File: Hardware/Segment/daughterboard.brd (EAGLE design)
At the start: 210.8 x 51.8 mm, 162 parts, among them IC1 PBQ79656PAPTQ1, IC2 PBQ79656PAPTQ1, T1 PBHV8115X, 115, T2 PBHV8115X, 115

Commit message: teensy.lbr
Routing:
- net CB5: track 53.4 -> 56.8 mm
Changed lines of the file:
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@@
 <attribute name="POPULARITY" value="73" x="174.117" y="67.31" size="1.778" layer="27" rot="R90" display="off"/>
 <attribute name="SPICEPREFIX" value="C" x="174.117" y="67.31" size="1.778" layer="27" rot="R90" display="off"/>
-<attribute name="VALUE" x="165.862" y="283.845" size="1.27" layer="27" rot="R90"/>
+<attribute name="VALUE" x="83.312" y="14.605" size="1.27" layer="27" rot="R90"/>
 </element>
 <element name="CAVDD" library="rcl" library_urn="urn:adsk.eagle:library:334" package="C0603" package3d_urn="urn:adsk.eagle:package:23616/2" value="1uf" x="85.725" y="18.415" smashed="yes" rot="R90">
@@
 <attribute name="POPULARITY" value="73" x="76.2" y="120.65" size="1.778" layer="27" rot="R180" display="off"/>
 <attribute name="SPICEPREFIX" value="C" x="76.2" y="120.65" size="1.778" layer="27" rot="R180" display="off"/>
-<attribute name="VALUE" x="-140.335" y="112.395" size="1.27" layer="27" rot="R180"/>
+<attribute name="VALUE" x="123.825" y="32.385" size="1.27" layer="27" rot="R180"/>
 </element>
 <element name="CAVDD-1" library="rcl" library_urn="urn:adsk.eagle:library:334" package="C0603" package3d_urn="urn:adsk.eagle:package:23616/2" value="1uf" x="125.095" y="33.655" smashed="yes">
@@
 <wire x1="68.453" y1="13.843" x2="67.6186" y2="14.9314" width="0.1524" layer="1"/>
 <wire x1="67.6186" y1="14.9314" x2="67.6186" y2="14.9946875" width="0.1524" layer="1"/>
-<wire x1="67.6186" y1="14.9946875" x2="66.04" y2="16.5732875" width="0.1524" layer="1"/>
-<wire x1="66.04" y1="24.55" x2="66.89" y2="25.4" width="0.1524" layer="1"/>
-<wire x1="66.04" y1="16.5732875" x2="66.04" y2="24.55" width="0.1524" layer="1"/>
+<wire x1="67.6186" y1="14.9946875" x2="62.05164375" y2="20.56164375" width="0.1524" layer="1"/>
+<wire x1="62.05164375" y1="20.56164375" x2="66.89" y2="25.4" width="0.1524" layer="1"/>
 </signal>
 <signal name="VC6">

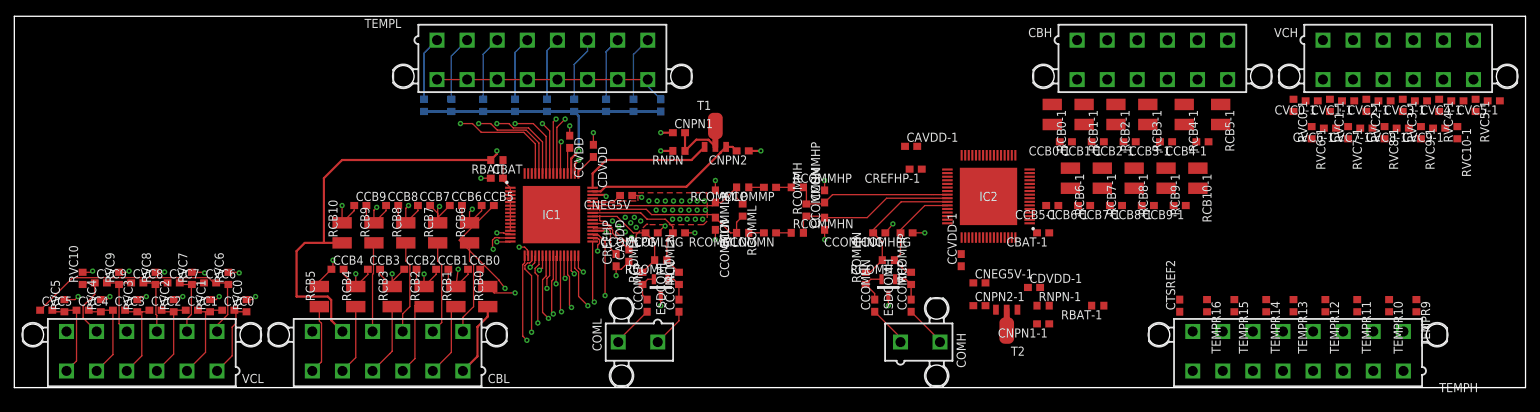
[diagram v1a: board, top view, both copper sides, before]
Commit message: Ground planes on segment
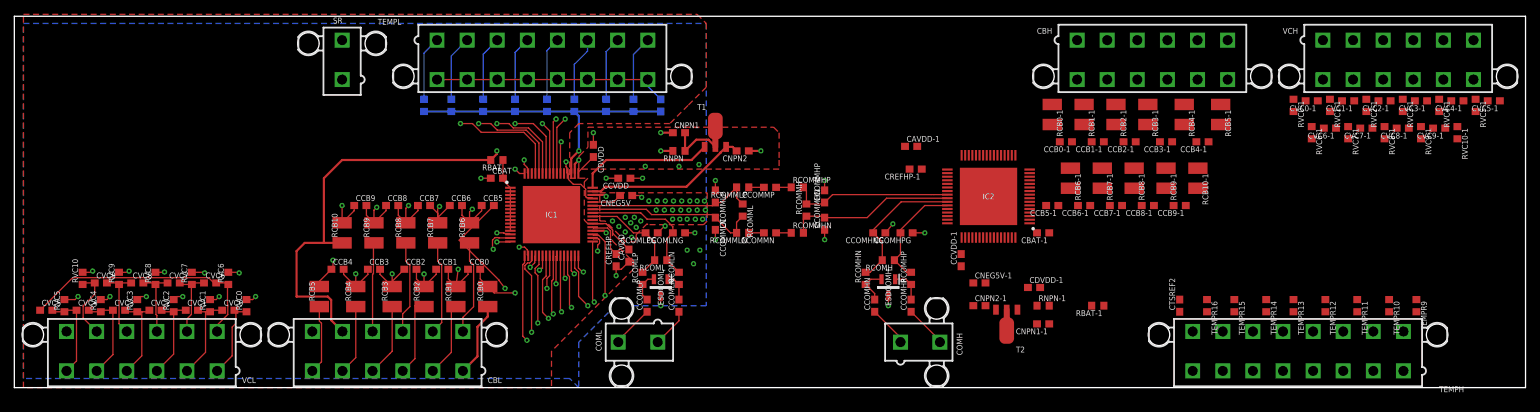
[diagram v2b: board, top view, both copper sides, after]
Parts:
- added SR: 5566-2, con-molex:5566-2
- moved CCVDD 9.16 mm to (85.1, 29.2), turned to 180 degrees
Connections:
- removed net GND: CNPN1.1, ESDCOML.3
- removed net GND-1: CNPN1-1.1, ESDCOMH.3
- removed net GND1: CBAT.1, CBL.1, CTSREF1.1, RCB0.1, TEMPL.10, TEMPL.11, TEMPL.12, TEMPL.13, TEMPL.14, TEMPL.15, TEMPL.16, TEMPL.9
- removed net GND1-1: CBAT-1.1, CBH.1, CTSREF2.1, RCB0-1.1, TEMPH.10, TEMPH.11, TEMPH.12, TEMPH.13, TEMPH.14, TEMPH.15, TEMPH.16, TEMPH.9
- removed net GNDN: CAVDD.1, CCOMLNG.1, CCOMLPG.1, CCOMMLN.2, CCOMMLP.1, CCVDD.1, CDVDD.1, CNEG5V.1, CNPN2.1, CREFHP.1, IC1.36, IC1.39, IC1.46, IC1.50, IC1.65
- removed net GNDN-1: CAVDD-1.1, CCOMHNG.1, CCOMHPG.1, CCOMMHN.1, CCOMMHP.2, CCVDD-1.1, CDVDD-1.1, CNEG5V-1.1, CNPN2-1.1, CREFHP-1.1, IC2.36, IC2.39, IC2.46, IC2.50, IC2.65
- new net GNDH: CAVDD-1.1, CBAT-1.1, CBH.1, CCOMHNG.1, CCOMHPG.1, CCOMMHN.1, CCOMMHP.2, CCVDD-1.1, CDVDD-1.1, CNEG5V-1.1, CNPN1-1.1, CNPN2-1.1, CREFHP-1.1, CTSREF2.1, ESDCOMH.3, IC2.36, IC2.39, IC2.46, IC2.50, IC2.65, RCB0-1.1, TEMPH.10, TEMPH.11, TEMPH.12, TEMPH.13, TEMPH.14, TEMPH.15, TEMPH.16, TEMPH.9
- new net GNDL: CAVDD.1, CBAT.1, CBL.1, CCOMLNG.1, CCOMLPG.1, CCOMMLN.2, CCOMMLP.1, CCVDD.1, CDVDD.1, CNEG5V.1, CNPN1.1, CNPN2.1, CREFHP.1, CTSREF1.1, ESDCOML.3, IC1.36, IC1.39, IC1.46, IC1.50, IC1.65, RCB0.1, TEMPL.10, TEMPL.11, TEMPL.12, TEMPL.13, TEMPL.14, TEMPL.15, TEMPL.16, TEMPL.9
- new net N$4: IC1.64, SR.1
- new net N$7: IC1.63, SR.2
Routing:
- net GNDL: track 0.00 -> 69.4 mm, vias 0 -> 50
- net GND1: track 44.7 -> 0.00 mm, vias 1 -> 0
- net N$7: track 0.00 -> 34.5 mm, vias 0 -> 1
- net N$4: track 0.00 -> 30.9 mm, vias 0 -> 1
- net GNDN: track 21.3 -> 0.00 mm, vias 41 -> 0
- net CVDD: track 3.69 -> 15.9 mm, vias 0 -> 2
- net GNDH: track 0.00 -> 7.46 mm, vias 0 -> 5
- net GNDN-1: track 6.07 -> 0.00 mm, vias 4 -> 0
- net GND: track 3.08 -> 0.00 mm, vias 2 -> 0
- net GND-1: track 1.39 -> 0.00 mm, vias 1 -> 0
- added copper zone on layer 1, net GNDL
- added copper zone on layer 16, net GNDL
- added copper zone on layer 2, net GNDL
- removed copper zone on layer 1, net GNDN
- removed copper zone on layer 2, net GNDN

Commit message: Board and schematic are consistent, mostly wired, some problems
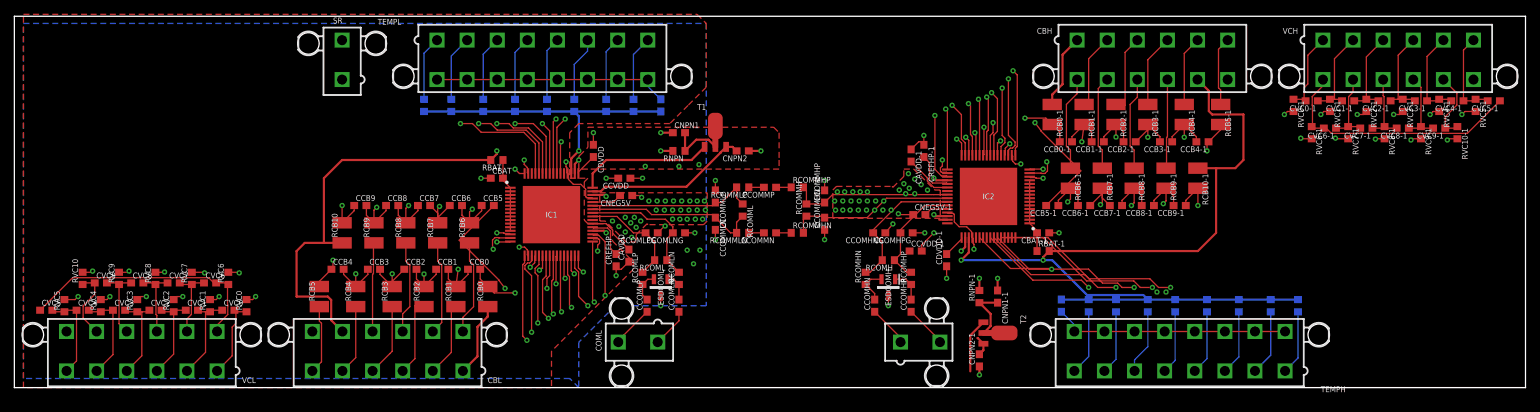
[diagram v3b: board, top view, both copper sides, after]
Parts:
- moved TEMPR10 16.5 mm to (175.3, 11.4), flipped to the bottom
- moved TEMPR15 16.5 mm to (153.7, 11.4), flipped to the bottom
- moved TEMPR9 16.5 mm to (179.1, 11.4), flipped to the bottom
- moved CTSREF2 16.5 mm to (146.1, 11.4), flipped to the bottom
- moved TEMPH 16.5 mm to (162.6, 5.08)
- moved TEMPR11 16.5 mm to (170.8, 11.4), flipped to the bottom
- moved TEMPR12 16.5 mm to (166.4, 11.4), flipped to the bottom
- moved TEMPR13 16.5 mm to (161.9, 11.4), flipped to the bottom
- moved TEMPR14 16.5 mm to (158.1, 11.4), flipped to the bottom
- moved TEMPR16 16.5 mm to (149.9, 11.4), flipped to the bottom
- moved CDVDD-1 12.8 mm to (130.0, 17.8), turned to 90 degrees
- moved CNEG5V-1 12.7 mm to (126.2, 24.1)
- moved RBAT-1 10.8 mm to (143.5, 19.1), turned to 0 degrees
- moved RNPN-1 8.98 mm to (134.6, 12.7), turned to 90 degrees
- moved CNPN2-1 7.62 mm to (134.6, 3.81), turned to 90 degrees
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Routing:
- net VC6-1: track 0.00 -> 108.8 mm, vias 0 -> 2
- net VC7-1: track 0.00 -> 106.6 mm, vias 0 -> 2
- net VC8-1: track 0.00 -> 97.7 mm, vias 0 -> 2
- net VC9-1: track 0.00 -> 94.5 mm, vias 0 -> 2
- net VC5-1: track 0.00 -> 77.7 mm, vias 0 -> 2
- net VC4-1: track 0.00 -> 73.2 mm, vias 0 -> 2
- net BATC-1: track 0.00 -> 70.4 mm, vias 0 -> 2
- net VC3-1: track 0.00 -> 68.8 mm, vias 0 -> 2
- net VC2-1: track 0.00 -> 66.2 mm, vias 0 -> 2
- net TSREF-1: track 0.00 -> 64.9 mm, vias 0 -> 1
- net TEMP9: track 0.00 -> 63.0 mm, vias 0 -> 1
- net VC1-1: track 0.00 -> 62.6 mm, vias 0 -> 2
- net VC10-1: track 0.00 -> 62.6 mm, vias 0 -> 2
- net GNDH: track 7.46 -> 68.4 mm, vias 5 -> 43
- net VC0-1: track 0.00 -> 60.0 mm, vias 0 -> 2
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- added copper zone on layer 1, net GNDH

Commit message: Almost done with daughter board
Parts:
- moved CNEG5V-1 1.71 mm to (127.5, 23.0)
- moved CDVDD-1 0.89 mm to (130.9, 17.8)
- moved CAVDD 0.25 mm to (86.0, 18.4)
- moved CAVDD-1 0.25 mm to (124.8, 32.4)
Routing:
- net TEMP14: track 21.8 -> 50.7 mm
- net TEMP15: track 24.4 -> 47.6 mm
- net LDOIN-1: track 3.99 -> 22.3 mm
- net TSREF-1: track 64.9 -> 52.9 mm
- net GNDH: track 68.4 -> 80.2 mm, vias 43 -> 39
- net NPNB-1: track 7.61 -> 16.5 mm
- net TEMP13: track 45.1 -> 51.4 mm
- net GNDL: track 69.4 -> 75.7 mm
- net TEMP12: track 48.1 -> 52.2 mm
- net CB5-1: track 56.8 -> 53.3 mm
- net CB5: track 56.8 -> 53.3 mm
- net TEMP10: track 60.0 -> 62.9 mm
- net TEMP9: track 63.0 -> 65.3 mm
- net N$113: track 3.39 -> 4.89 mm
- net TEMP16: track 39.1 -> 40.2 mm
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- added copper zone on layer 16, net GNDH
- added copper zone on layer 2, net GNDH

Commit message: No more airwires!
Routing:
- net GNDH: vias 39 -> 47
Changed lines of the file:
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@@
 <via x="125.73" y="27.559" extent="1-16" drill="0.35"/>
 <via x="138.43" y="3.81" extent="1-16" drill="0.35"/>
-<wire x1="127.381" y1="27.559" x2="130.152" y2="27.42" width="0" layer="19" extent="1-1"/>
+<via x="115.57" y="22.86" extent="1-2" drill="0.35"/>
+<via x="116.84" y="22.86" extent="1-2" drill="0.35"/>
+<via x="118.11" y="22.86" extent="1-2" drill="0.35"/>
+<via x="123.19" y="24.13" extent="1-2" drill="0.35"/>
+<via x="123.825" y="25.019" extent="1-2" drill="0.35"/>
+<via x="125.222" y="25.019" extent="1-2" drill="0.35"/>
+<via x="124.46" y="24.13" extent="1-2" drill="0.35"/>
+<via x="140.843" y="21.971" extent="1-16" drill="0.35"/>
 </signal>
 <signal name="N$131">
